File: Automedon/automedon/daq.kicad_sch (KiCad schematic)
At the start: 20 parts, among them J17 09-4224-00-04, J18 09-4224-00-04, J19 09-4224-00-04, J20 09-4224-00-04, J21 09-4224-00-04, J22 09-4224-00-04, J23 09-4224-00-04, J24 09-4224-00-04, J25 09-4224-00-04, J26 09-4224-00-04, J27 09-4224-00-04, J28 09-4224-00-04, U19 USB POWER, U20 DAQ PWR, U21 DAQ PWR, U22 DAQ PWR

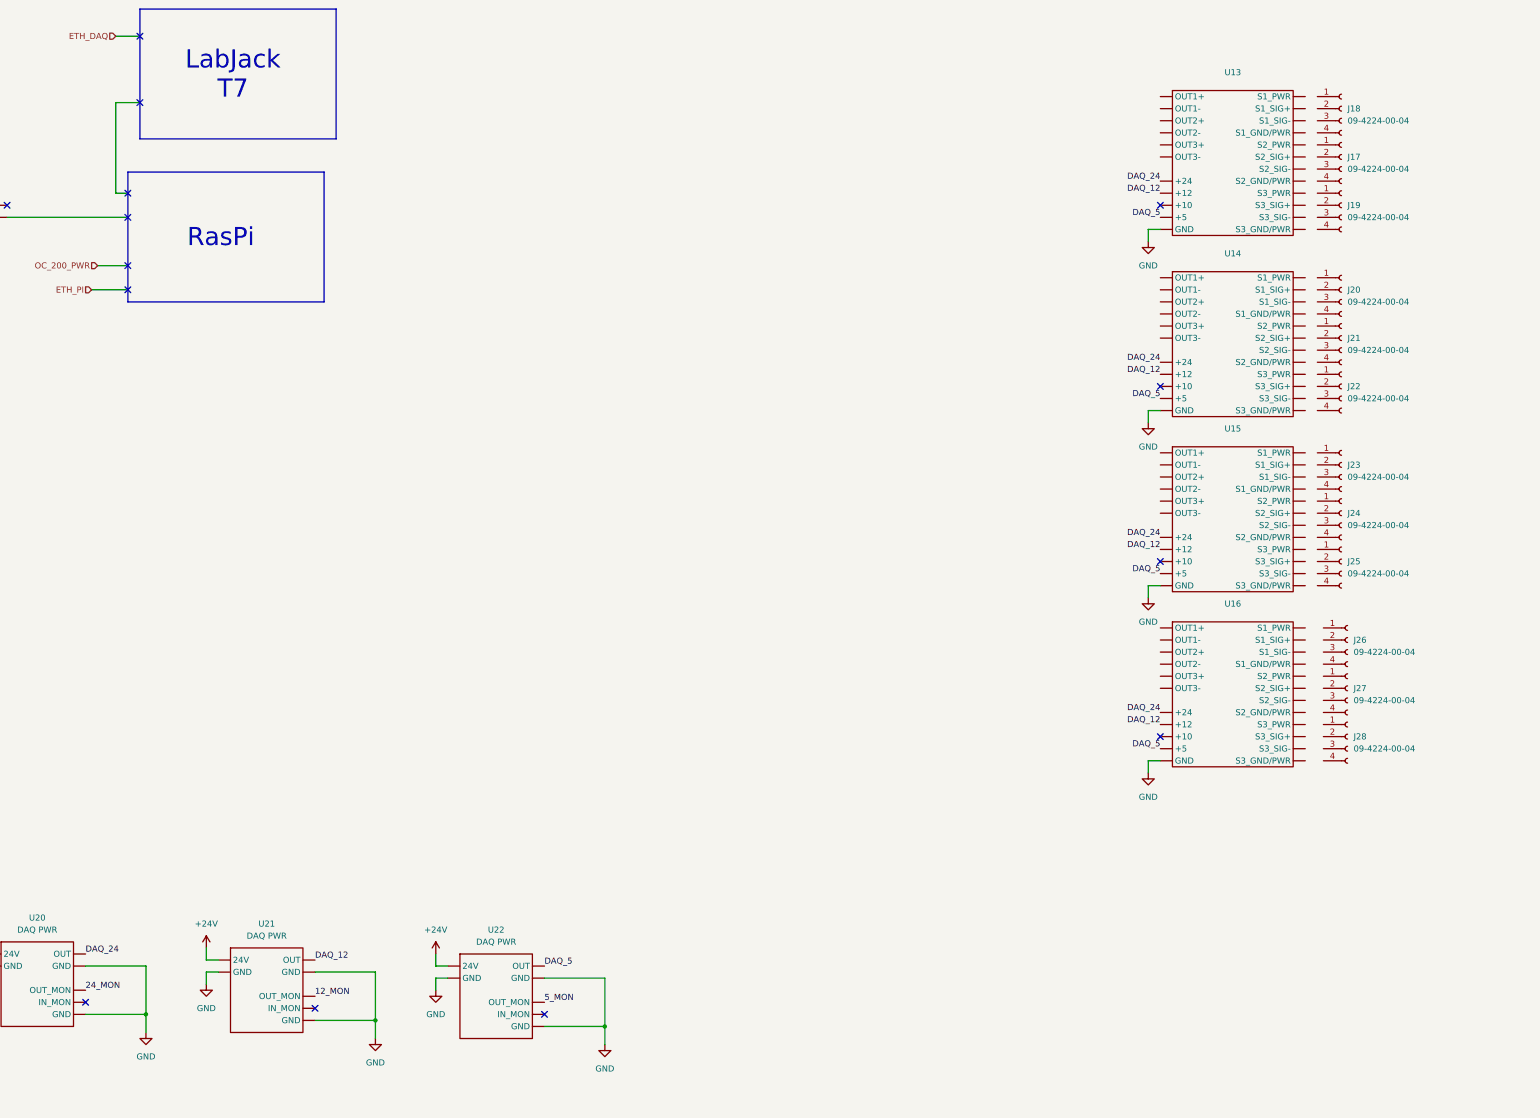
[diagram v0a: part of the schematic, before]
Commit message: Update eth ports
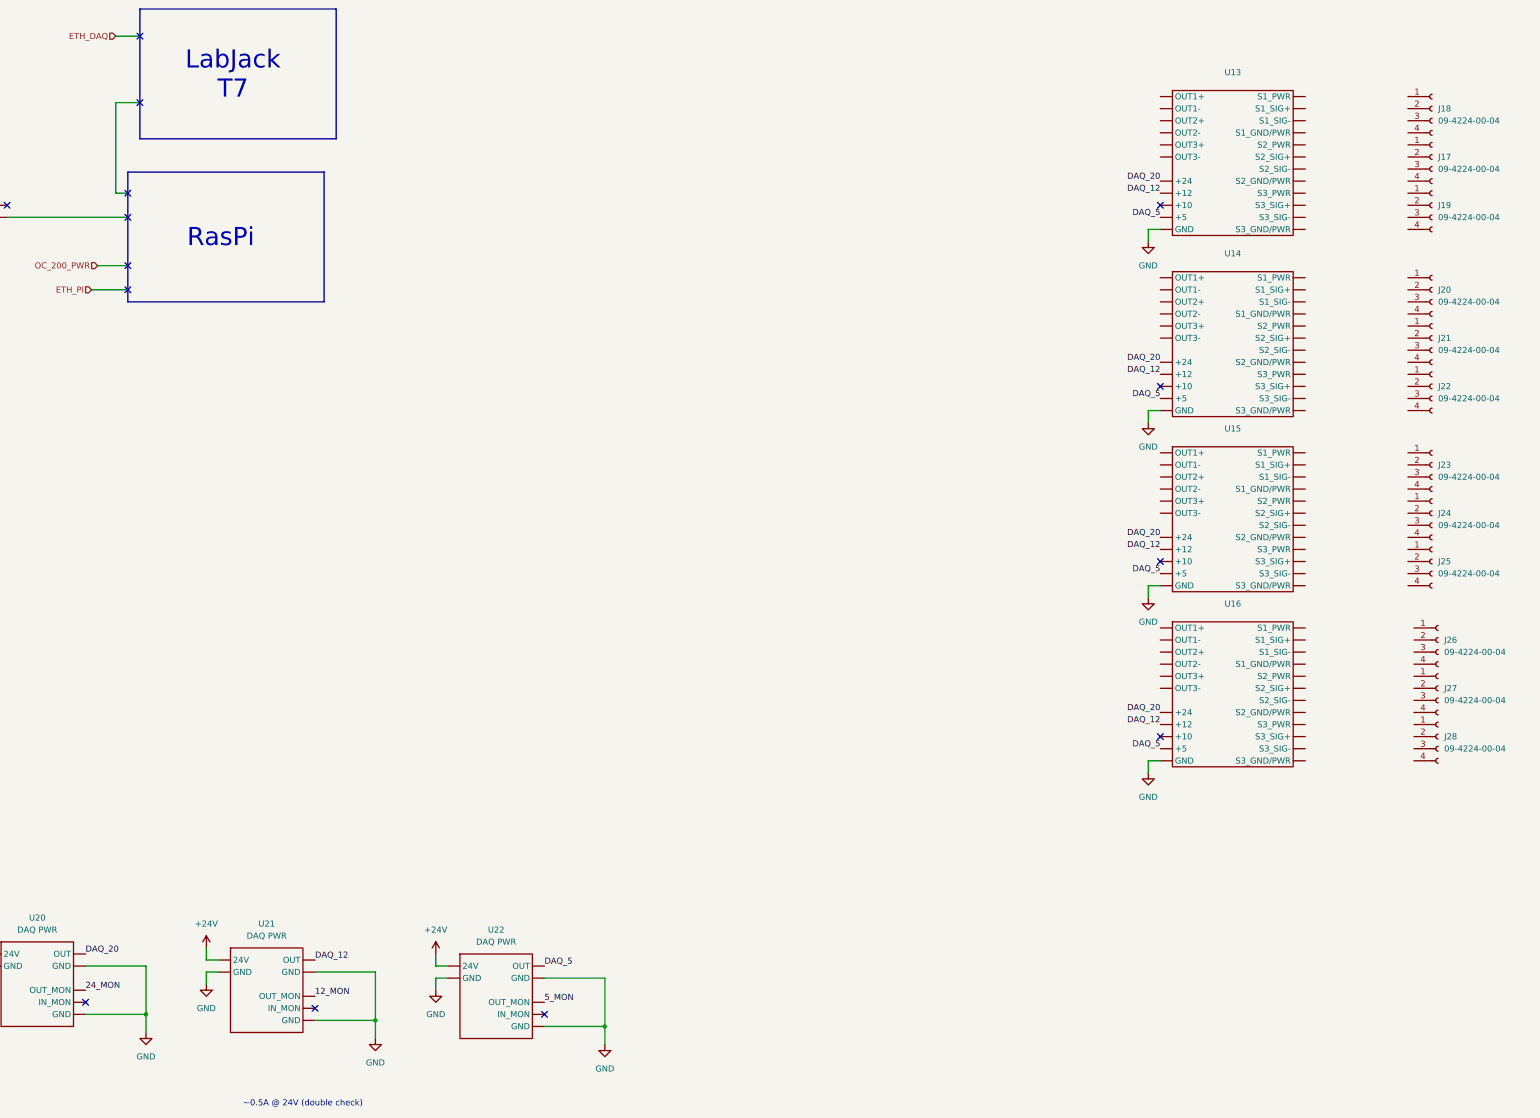
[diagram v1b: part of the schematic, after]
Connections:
- net DAQ_24 is gone; now on net GND: U13. (S3_GND/PWR), U14. (S3_GND/PWR), U15. (S3_GND/PWR), U16. (S3_GND/PWR), U20. (GND)
- new net DAQ_20: U13. (S3_GND/PWR), U14. (S3_GND/PWR), U15. (S3_GND/PWR), U16. (S3_GND/PWR), U20. (GND)
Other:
- note added: "~0.5A @ 24V (double check)"
- moved on the sheet: J17, J18, J19, J20, J21, J22, J23, J24, J25, J26, J27, J28

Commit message: Update a bunch of shit
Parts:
- added J54, J55, J56: 09-4224-00-04, symbol Connector:Conn_01x04_Socket
- added R1, R2, R3, R4: 100k, symbol Device:R_US
- added TC1, TC2, TC5, TC6: K1, symbol Device:Thermocouple_Block
- added U27: USB PWR, symbol automedon:USB_PWR_A
- added U28: ~, symbol automedon:patch_panel
- added U29, U30, U31: CB37, symbol automedon:CB37
- added U32: LM34CAZ, Package_TO_SOT_THT:TO-92_Inline, symbol Sensor_Temperature:LM35-LP
- added U33, U34: DAQ CAN, symbol automedon:DAQ_CAN
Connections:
- net 24_MON is gone; now on net GNDA: U20. (GND)
- net +12V: now also U27. (USB_A2)
- net 12_MON: now also U30.12 (AIN13)
- net DAQ_12: now also U28. (S3_GND/PWR)
- net DAQ_20: now also U28. (S3_GND/PWR)
- net DAQ_5: now also U28. (S3_GND/PWR)
- net GND: now also U27. (USB_A2); no longer U13. (S3_GND/PWR), U14. (S3_GND/PWR), U15. (S3_GND/PWR), U16. (S3_GND/PWR)
- net OC_200_PWR: now also U27. (USB_A2)
- net at J27.1 (Pin_1): now also U16. (S3_GND/PWR)
- net at J27.2 (Pin_2): now also U16. (S3_GND/PWR)
- net at J27.3 (Pin_3): now also U16. (S3_GND/PWR)
- net at J27.4 (Pin_4): now also U16. (S3_GND/PWR)
- net at J22.1 (Pin_1): now also U14. (S3_GND/PWR)
- net at J22.2 (Pin_2): now also U14. (S3_GND/PWR)
- net at J22.3 (Pin_3): now also U14. (S3_GND/PWR)
- net at J22.4 (Pin_4): now also U14. (S3_GND/PWR)
- net GNDA: now reaches U21. (GND)
- net GNDA: now also U13. (S3_GND/PWR), U14. (S3_GND/PWR), U15. (S3_GND/PWR), U16. (S3_GND/PWR), U22. (GND), U28. (S3_GND/PWR), U29.19 (GND), U30.19 (GND), U31.19 (GND)
- net at J26.1 (Pin_1): now also U16. (S3_GND/PWR)
- net at J26.2 (Pin_2): now also U16. (S3_GND/PWR)
- net at J26.3 (Pin_3): now also U16. (S3_GND/PWR)
- net at J26.4 (Pin_4): now also U16. (S3_GND/PWR)
- net at J17.1 (Pin_1): now also U13. (S3_GND/PWR)
- net at J17.2 (Pin_2): now also U13. (S3_GND/PWR)
- net at J17.3 (Pin_3): now also U13. (S3_GND/PWR)
- net at J17.4 (Pin_4): now also U13. (S3_GND/PWR)
- net at J28.1 (Pin_1): now also U16. (S3_GND/PWR)
- net at J28.2 (Pin_2): now also U16. (S3_GND/PWR)
- net at J28.3 (Pin_3): now also U16. (S3_GND/PWR)
- net at J28.4 (Pin_4): now also U16. (S3_GND/PWR)
- net at J23.1 (Pin_1): now also U15. (S3_GND/PWR)
- net at J23.2 (Pin_2): now also U15. (S3_GND/PWR)
- net at J23.3 (Pin_3): now also U15. (S3_GND/PWR)
- net at J23.4 (Pin_4): now also U15. (S3_GND/PWR)
- net at J20.1 (Pin_1): now also U14. (S3_GND/PWR)
- net at J20.2 (Pin_2): now also U14. (S3_GND/PWR)
- net at J20.3 (Pin_3): now also U14. (S3_GND/PWR)
- net at J20.4 (Pin_4): now also U14. (S3_GND/PWR)
- net at J25.1 (Pin_1): now also U15. (S3_GND/PWR)
- net at J25.2 (Pin_2): now also U15. (S3_GND/PWR)
- net at J25.3 (Pin_3): now also U15. (S3_GND/PWR)
- net at J25.4 (Pin_4): now also U15. (S3_GND/PWR)
- net at J24.1 (Pin_1): now also U15. (S3_GND/PWR)
- net at J24.2 (Pin_2): now also U15. (S3_GND/PWR)
- net at J24.3 (Pin_3): now also U15. (S3_GND/PWR)
- net at J24.4 (Pin_4): now also U15. (S3_GND/PWR)
- net at J19.1 (Pin_1): now also U13. (S3_GND/PWR)
- net at J19.2 (Pin_2): now also U13. (S3_GND/PWR)
- net at J19.3 (Pin_3): now also U13. (S3_GND/PWR)
- net at J19.4 (Pin_4): now also U13. (S3_GND/PWR)
- net at J18.1 (Pin_1): now also U13. (S3_GND/PWR)
- net at J18.2 (Pin_2): now also U13. (S3_GND/PWR)
- net at J18.3 (Pin_3): now also U13. (S3_GND/PWR)
- net at J18.4 (Pin_4): now also U13. (S3_GND/PWR)
- net at J21.1 (Pin_1): now also U14. (S3_GND/PWR)
- net at J21.2 (Pin_2): now also U14. (S3_GND/PWR)
- net at J21.3 (Pin_3): now also U14. (S3_GND/PWR)
- net at J21.4 (Pin_4): now also U14. (S3_GND/PWR)
- new net: U30.27 (Vs), U32.1 (+V_{S})
- new net: U30.19 (GND), U32.2 (GND)
- new net: U30.31 (AIN12), U32.3 (V_{OUT})
- new net: TC1.1 (+), U30.15 (AIN7)
- new net: TC5.1 (+), U30.16 (AIN5)
- new net: TC6.1 (+), U30.17 (AIN3)
- new net: TC2.1 (+), U30.18 (AIN1)
- new net: R4.2, U30.19 (GND)
- new net: R1.2, U30.19 (GND)
- new net: R3.2, U30.19 (GND)
- new net: R2.2, U30.19 (GND)
- new net: R1.1, TC1.2 (-), U30.34 (AIN6)
- new net: R2.1, TC5.2 (-), U30.35 (AIN4)
- new net: R3.1, TC6.2 (-), U30.36 (AIN2)
- new net: R4.1, TC2.2 (-), U30.37 (AIN0)
- new net: U13. (S3_GND/PWR), U29.12 (AIN13)
- new net: U13. (S3_GND/PWR), U29.13 (AIN11)
- new net: U13. (S3_GND/PWR), U29.14 (AIN9)
- new net: U14. (S3_GND/PWR), U29.15 (AIN7)
- new net: U14. (S3_GND/PWR), U29.16 (AIN5)
- new net: U14. (S3_GND/PWR), U29.17 (AIN3)
- new net: U15. (S3_GND/PWR), U29.18 (AIN1)
- new net: U13. (S3_GND/PWR), U29.31 (AIN12)
- new net: U13. (S3_GND/PWR), U29.32 (AIN10)
- new net: U13. (S3_GND/PWR), U29.33 (AIN8)
- new net: U14. (S3_GND/PWR), U29.34 (AIN6)
- new net: U14. (S3_GND/PWR), U29.35 (AIN4)
- new net: U14. (S3_GND/PWR), U29.36 (AIN2)
- new net: U15. (S3_GND/PWR), U29.37 (AIN0)
- new net: J54.1 (Pin_1), U28. (S3_GND/PWR)
- new net: J54.2 (Pin_2), U28. (S3_GND/PWR)
- new net: J54.3 (Pin_3), U28. (S3_GND/PWR)
- new net: J54.4 (Pin_4), U28. (S3_GND/PWR)
- new net: J56.1 (Pin_1), U28. (S3_GND/PWR)
- new net: J56.2 (Pin_2), U28. (S3_GND/PWR)
- new net: J56.3 (Pin_3), U28. (S3_GND/PWR)
- new net: J56.4 (Pin_4), U28. (S3_GND/PWR)
- new net: U28. (S3_GND/PWR), U31.17 (AIN3)
- new net: U28. (S3_GND/PWR), U31.18 (AIN1)
- new net: U28. (S3_GND/PWR), U31.36 (AIN2)
- new net: U28. (S3_GND/PWR), U31.37 (AIN0)
- new net: J55.1 (Pin_1), U28. (S3_GND/PWR)
- new net: J55.2 (Pin_2), U28. (S3_GND/PWR)
- new net: J55.3 (Pin_3), U28. (S3_GND/PWR)
- new net: J55.4 (Pin_4), U28. (S3_GND/PWR)
- new net: U15. (S3_GND/PWR), U31.12 (AIN13)
- new net: U15. (S3_GND/PWR), U31.13 (AIN11)
- new net: U16. (S3_GND/PWR), U31.14 (AIN9)
- new net: U16. (S3_GND/PWR), U31.15 (AIN7)
- new net: U16. (S3_GND/PWR), U31.16 (AIN5)
- new net: U15. (S3_GND/PWR), U31.31 (AIN12)
- new net: U15. (S3_GND/PWR), U31.32 (AIN10)
- new net: U16. (S3_GND/PWR), U31.33 (AIN8)
- new net: U16. (S3_GND/PWR), U31.34 (AIN6)
- new net: U16. (S3_GND/PWR), U31.35 (AIN4)
- new net 12_BUS_MON: U30.32 (AIN10)
- new net 20_MON: U20. (GND), U30.13 (AIN11)
- new net 24_BUS: U30.14 (AIN9)
- new net 5V_BUS: U30.33 (AIN8)
- new net DAQ_CAN_1: U27. (USB_A2), U33. (CANL)
- new net DAQ_CAN_2: U27. (USB_A2), U34. (CANL)
- new net USB_DAQ: U27. (USB_A2)
- no-connect marks 14 -> 140
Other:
- moved on the sheet: J17, J18, J19, J20, J21, J22, J23, J24, J25, U13, U14, U15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
